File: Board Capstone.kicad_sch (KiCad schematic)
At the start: 28 parts, among them J101 JST-ZH 4P, J102 HDR 02x20 2.54, J103 JST-ZH 2P, J104 JST-ZH 2P, J105 JST-ZH 3P, J106 JST-ZH 3P, Q101 FDV304P, Q102 BC847CLT3G, Q103 MMBT2907AL, Q104 MMBT2907AL, U101 MCP3021, U102 SN74LV1T125DBV, U103 SN74LV1T125DBV

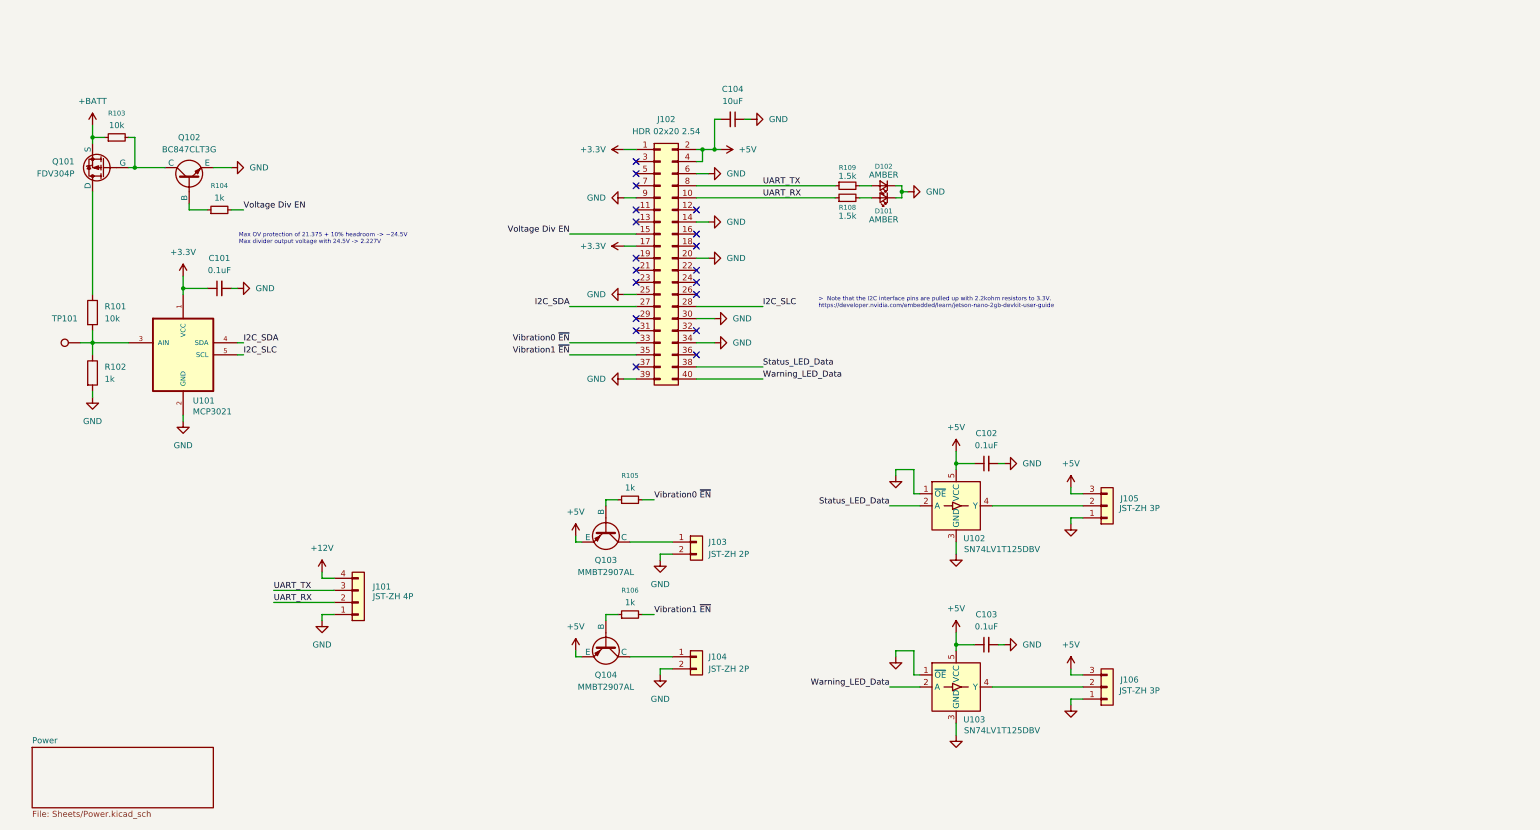
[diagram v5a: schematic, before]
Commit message: Rev 2.3 New battery protection IC and various other changes
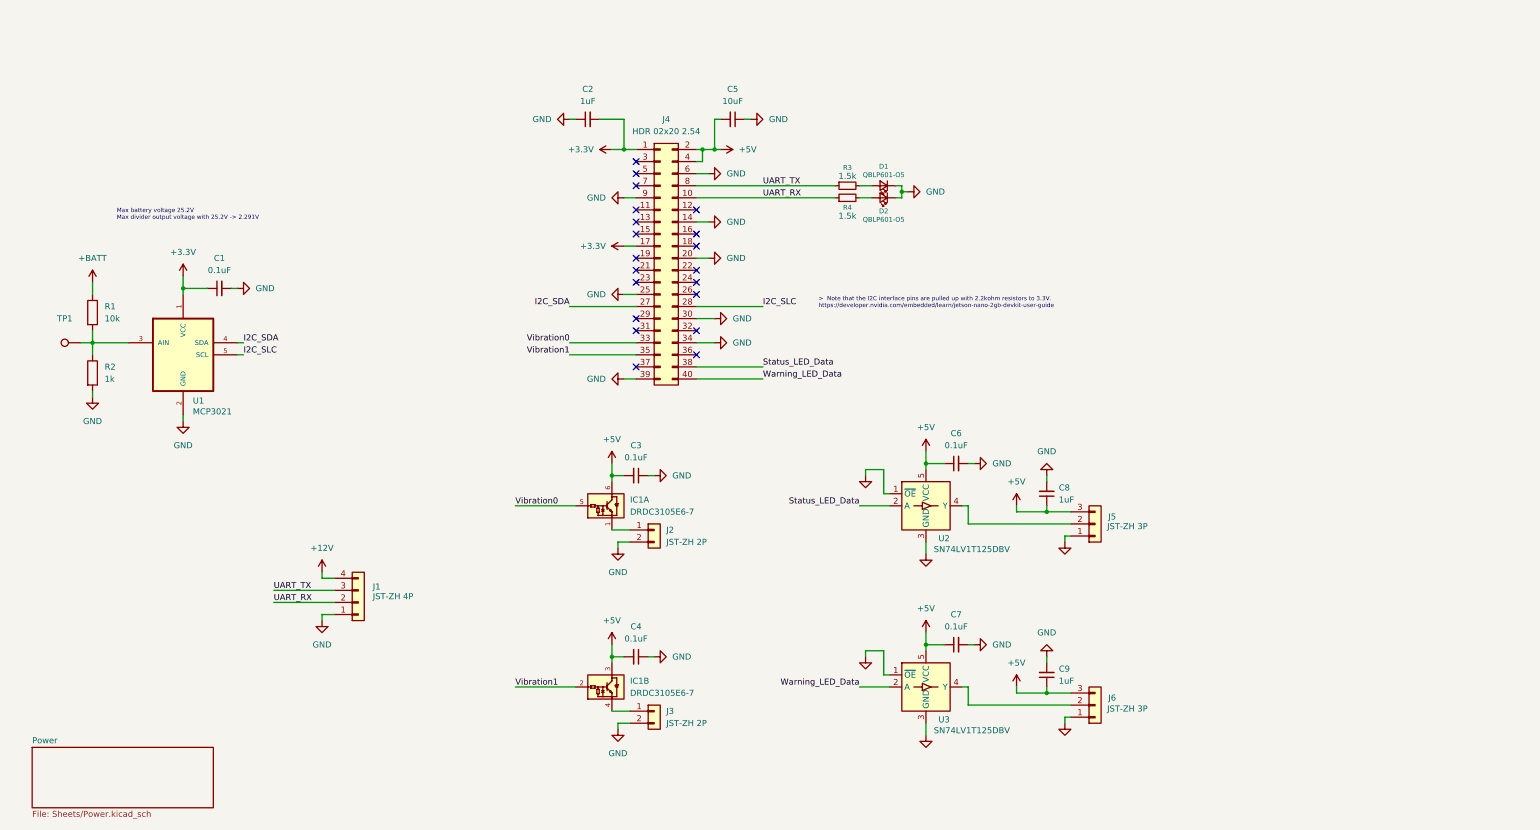
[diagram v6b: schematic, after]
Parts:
- removed Q101: FDV304P, Package_TO_SOT_SMD:SOT-23-3, symbol Simulation_SPICE:PMOS
- removed Q102: BC847CLT3G, Package_TO_SOT_SMD:SOT-23, symbol Simulation_SPICE:NPN
- removed Q103, Q104: MMBT2907AL, Package_TO_SOT_SMD:SOT-23, symbol Simulation_SPICE:PNP
- removed R103: 10k, Resistor_SMD:R_1206_3216Metric_Pad1.30x1.75mm_HandSolder, symbol Device:R_Small
- removed R104, R105, R106: 1k, Resistor_SMD:R_1206_3216Metric_Pad1.30x1.75mm_HandSolder, symbol Device:R_Small
- added C2, C8, C9: 1uF, Capacitor_SMD:C_1206_3216Metric_Pad1.33x1.80mm_HandSolder, symbol Device:C_Small
- added C3, C4: 0.1uF, Capacitor_SMD:C_1206_3216Metric_Pad1.33x1.80mm_HandSolder, symbol Device:C_Small
- added IC1: DRDC3105E6-7, Package_TO_SOT_SMD:SOT-23-6, symbol drdc3105:DRDC3105E6-7
- D1: renamed from D102; value AMBER -> QBLP601-O5
- D2: renamed from D101; value AMBER -> QBLP601-O5
- renumbered C101 to C1, C104 to C5, C102 to C6, C103 to C7, J101 to J1, J103 to J2, J104 to J3, J102 to J4, J105 to J5, J106 to J6, R101 to R1, R102 to R2, R109 to R3, R108 to R4, TP101 to TP1, U101 to U1, U102 to U2, U103 to U3
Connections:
- net +3.3V: now also C2.2
- net +5V: now also C3.2, C4.2, C8.1, C9.1, IC1.3, IC1.6
- net +BATT: now also R1.1
- net GND: now also C2.1, C3.1, C4.1, C8.2, C9.2
- net at J2.1 (Pin_1): now also IC1.1
- net at J3.1 (Pin_1): now also IC1.4
- net Vibration0 ~{EN} renamed Vibration0
- net Vibration0: now also IC1.5
- net Vibration1 ~{EN} renamed Vibration1
- net Vibration1: now also IC1.2
- net Voltage Div EN: no longer names the net of J4.15 (Pin_15)
- no-connect marks 19 -> 20
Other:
- note added: "Max battery voltage 25.2V Max divider output voltage with 25.2V -> 2.291V"
- note removed: "Max OV protection of 21.375 + 10% headroom -> ~24.5V Max divider output voltage with 24.5V -> 2.227V"
- moved on the sheet: C6, C7, J2, J3, J5, J6, U2, U3

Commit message: Rev 2.4
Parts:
- removed D1, D2: QBLP601-O5, LED_SMD:LED_0603_1608Metric_Pad1.05x0.95mm_HandSolder, symbol Device:LED_Small
- removed IC1: DRDC3105E6-7, Package_TO_SOT_SMD:SOT-23-6, symbol drdc3105:DRDC3105E6-7
- added C1: 10uF, Capacitor_SMD:C_0805_2012Metric_Pad1.18x1.45mm_HandSolder, symbol Device:C_Small
- added C29: 1uF, Capacitor_SMD:C_0805_2012Metric_Pad1.18x1.45mm_HandSolder, symbol Device:C_Small
- added D10: D_Zener, Diode_SMD:D_0805_2012Metric_Pad1.15x1.40mm_HandSolder, symbol Device:D_Zener
- added JP1, JP2: SolderJumper_2_Open, Jumper:SolderJumper-2_P1.3mm_Open_RoundedPad1.0x1.5mm, symbol Jumper:SolderJumper_2_Open
- added U2, U3: TPS22917DBV, Package_TO_SOT_SMD:SOT-23-6, symbol Power_Management:TPS22917DBV
- C10: renamed from C9; footprint Capacitor_SMD:C_1206_3216Metric_Pad1.33x1.80mm_HandSolder -> Capacitor_SMD:C_0805_2012Metric_Pad1.18x1.45mm_HandSolder
- C2: renamed from C1; footprint Capacitor_SMD:C_1206_3216Metric_Pad1.33x1.80mm_HandSolder -> Capacitor_SMD:C_0805_2012Metric_Pad1.18x1.45mm_HandSolder
- C3, C4: value 0.1uF -> 1uF; footprint Capacitor_SMD:C_1206_3216Metric_Pad1.33x1.80mm_HandSolder -> Capacitor_SMD:C_0805_2012Metric_Pad1.18x1.45mm_HandSolder
- C5: renamed from C2; footprint Capacitor_SMD:C_1206_3216Metric_Pad1.33x1.80mm_HandSolder -> Capacitor_SMD:C_0805_2012Metric_Pad1.18x1.45mm_HandSolder
- C6: renamed from C5; footprint Capacitor_SMD:C_1206_3216Metric_Pad1.33x1.80mm_HandSolder -> Capacitor_SMD:C_0805_2012Metric_Pad1.18x1.45mm_HandSolder
- C7: renamed from C6; footprint Capacitor_SMD:C_1206_3216Metric_Pad1.33x1.80mm_HandSolder -> Capacitor_SMD:C_0805_2012Metric_Pad1.18x1.45mm_HandSolder
- C8: renamed from C7; footprint Capacitor_SMD:C_1206_3216Metric_Pad1.33x1.80mm_HandSolder -> Capacitor_SMD:C_0805_2012Metric_Pad1.18x1.45mm_HandSolder
- C9: renamed from C8; footprint Capacitor_SMD:C_1206_3216Metric_Pad1.33x1.80mm_HandSolder -> Capacitor_SMD:C_0805_2012Metric_Pad1.18x1.45mm_HandSolder
- R1, R2: footprint Resistor_SMD:R_1206_3216Metric_Pad1.30x1.75mm_HandSolder -> Resistor_SMD:R_0805_2012Metric_Pad1.20x1.40mm_HandSolder
- R3, R4: value 1.5k -> 680; footprint Resistor_SMD:R_1206_3216Metric_Pad1.30x1.75mm_HandSolder -> Resistor_SMD:R_0805_2012Metric_Pad1.20x1.40mm_HandSolder
- TP1: footprint TestPoint:TestPoint_Pad_D2.5mm -> TestPoint:TestPoint_Pad_D1.5mm
- renumbered U2 to U4, U3 to U5
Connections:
- net +12V: now also C1.2
- net +5V: now also U2.1 (VIN), U3.1 (VIN)
- net GND: now also C1.1, C29.1, D10.2 (A), U2.2 (GND), U3.2 (GND)
- net I2C_SDA: now also JP2.2 (B)
- net I2C_SLC: now also JP1.2 (B)
- net UART_RX: no longer R4.1
- net UART_TX: no longer R3.1
- net Vibration0: now also U2.3 (ON)
- net Vibration1: now also U3.3 (ON)
- net at J3.1 (Pin_1): now also R4.2, U3.6 (VOUT)
- net at R1.2, R2.1, TP1.1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: now also C29.2, D10.1 (K)
- net at J2.1 (Pin_1): now also R3.2, U2.6 (VOUT)
- new net: R4.1, U3.5 (QOD)
- new net: R3.1, U2.5 (QOD)
- new net Power/SCL: JP1.1 (A)
- new net Power/SDA: JP2.1 (A)
- no-connect marks 20 -> 22
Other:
- sheet Power ports: added SCL, SDA; removed none
- moved on the sheet: C2, C3, J1, J2, R1, R2, TP1, U1
